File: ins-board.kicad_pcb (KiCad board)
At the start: 4 copper layers, 50 x 23 mm, 93 parts, among them P1 POWER, Q1 FDN306P, Q2 FDC638APZ, U1 24LC128, U10 HMC5883L, U11 H3LIS331DL, U2 STM32F415RGT6, U3 LTC4412, U4 MAX3051, U5 LT1965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

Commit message: signal routing
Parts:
- R15: moved to F.Cu
- moved U4 7.37 mm to (66.9, 45.6)
- moved C11 2.70 mm to (70.2, 47.2), turned to 270 degrees
- moved R15 2.35 mm to (65.8, 47.1), turned to 0 degrees
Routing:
- net /STM32F4_NRST: track 0.00 -> 30.4 mm, vias 0 -> 2
- net /USB_DP: track 0.00 -> 15.8 mm, vias 0 -> 1
- net /V_USB: track 0.00 -> 15.5 mm, vias 0 -> 1
- net /USB_DM: track 0.00 -> 14.8 mm, vias 0 -> 1
- net /STM32F4_TMS: track 0.00 -> 12.9 mm, vias 0 -> 2
- net /Sensors/I2C_SCL: track 0.00 -> 12.7 mm, vias 0 -> 1
- net /Sensors/I2C_SDA: track 0.00 -> 11.4 mm, vias 0 -> 1
- net /UART_CONN3_TX: track 24.7 -> 20.8 mm, vias 1 -> 3
- net /UART_CONN3_RX: track 17.1 -> 19.8 mm, vias 0 -> 1
- net /CAN_CONN1_TX: track 0.00 -> 2.41 mm, vias 0 -> 1
- net /CAN_CONN1_RX: track 0.00 -> 0.99 mm, vias 0 -> 1
- net /Sensors/SPI_MISO: track 13.8 -> 14.7 mm
- net /Sensors/SPI_SCK: track 23.2 -> 22.3 mm
- net /Sensors/SPI_MOSI: track 23.0 -> 22.3 mm

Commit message: signal routing
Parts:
- moved R18 7.76 mm to (56.9, 47.5)
- moved C19 4.23 mm to (68.1, 46.9)
- moved C28 1.04 mm to (53.2, 44.2)
- moved U4 0.36 mm to (66.6, 45.8)
- moved C11 0.11 mm to (70.2, 47.4)
- moved R15 0.07 mm to (65.8, 47.1)
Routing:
- net N-0000059: track 0.00 -> 10.8 mm
- net /CAN_CONN1_RX: track 0.99 -> 10.3 mm
- net N-0000058: track 0.00 -> 9.27 mm
- net /Sensors/I2C_SDA: track 11.4 -> 18.5 mm
- net /CAN_CONN1_TX: track 2.41 -> 7.07 mm
- net N-000006: track 0.00 -> 4.40 mm, vias 0 -> 1
- net /Sensors/I2C_SCL: track 12.7 -> 16.9 mm
- net N-0000085: track 0.00 -> 3.75 mm, vias 0 -> 1
- net N-000003: track 3.16 -> 0.00 mm, vias 1 -> 0
- net /CAN_CONN1_EN: track 0.00 -> 1.93 mm

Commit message: signal routing
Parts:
- moved U4 1.82 mm to (66.0, 44.1)
- moved C19 1.57 mm to (67.5, 45.4)
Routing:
- net N-0000059: track 10.8 -> 0.00 mm
- net /CAN_CONN1_RX: track 10.3 -> 0.00 mm, vias 1 -> 0
- net N-0000058: track 9.27 -> 0.00 mm
- net /CAN_CONN1_TX: track 7.07 -> 0.00 mm, vias 1 -> 0
- net N-000006: track 4.40 -> 0.00 mm, vias 1 -> 0
- net /UART_CONN2_TX: track 20.1 -> 19.4 mm
- net /UART_CONN3_RX: track 19.8 -> 20.4 mm

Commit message: signal routing
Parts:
- R15: moved to B.Cu
- moved C11 3.91 mm to (72.7, 50.4)
- moved R15 0.66 mm to (65.7, 47.8)
- moved U4 0.54 mm to (66.2, 44.5)
- moved C19 0.49 mm to (67.7, 45.9)
- moved C6 0.30 mm to (70.0, 47.2), turned to 0 degrees
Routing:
- net /I2C_CONN1_SDA: track 0.00 -> 39.0 mm, vias 0 -> 2
- net /I2C_CONN1_SCL: track 0.00 -> 36.7 mm, vias 0 -> 2
- net N-0000058: track 0.00 -> 33.6 mm
- net N-0000059: track 0.00 -> 33.4 mm
- net /CAN_CONN1_RX: track 0.00 -> 10.2 mm, vias 0 -> 1
- net /CAN_CONN1_TX: track 0.00 -> 6.61 mm, vias 0 -> 1
- net N-000006: track 0.00 -> 4.15 mm
- net GND: track 40.1 -> 41.6 mm
- net VCC: track 14.6 -> 13.8 mm, vias 4 -> 3
- net /CAN_CONN1_EN: track 1.93 -> 2.69 mm, vias 0 -> 1

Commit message: signal routing
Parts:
- C11: moved to F.Cu
- moved C11 4.58 mm to (69.1, 47.5)
- moved C13 2.40 mm to (43.7, 41.5), turned to 180 degrees
- moved C6 0.57 mm to (70.5, 47.0), turned to 270 degrees
- moved F1 0.48 mm to (49.5, 31.4)
- moved C31 0.37 mm to (49.9, 44.9), turned to 0 degrees
- moved C28 0.28 mm to (53.0, 44.4)
- moved D6 0.16 mm to (47.1, 31.4)
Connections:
- U2 pad 26: /IO_EN -> /Sensors/HMC5883L_DRDY
- U2 pad 28: (no net) -> /IO_EN
- U2 pad 3: /Sensors/HMC5883L_DRDY -> (no net)
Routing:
- net /Sensors/HMC5883L_DRDY: track 0.00 -> 27.4 mm, vias 0 -> 2
- net /Sensors/I2C_SCL: track 16.9 -> 29.6 mm, vias 1 -> 2
- net /Sensors/I2C_SDA: track 18.5 -> 28.0 mm, vias 1 -> 5
- net N-0000077: track 2.43 -> 9.93 mm
- net GND: track 41.6 -> 46.1 mm, vias 7 -> 8
- net N-0000084: track 0.00 -> 2.58 mm, vias 0 -> 1
- net VCC: track 13.8 -> 16.3 mm, vias 3 -> 4
- net /V_USB: track 15.5 -> 17.3 mm, vias 1 -> 2
- net N-000003: track 0.00 -> 1.39 mm
- net N-0000085: track 3.75 -> 2.36 mm
- net /UART_CONN3_RX: track 20.4 -> 19.5 mm
- net /Sensors/MPU6000_FSYNC: track 11.4 -> 10.8 mm
- net /UART_CONN3_TX: track 21.1 -> 21.6 mm

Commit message: signal routing
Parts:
- D1, D3, D4, D5, R1, R7, R8, R9: moved to B.Cu
- moved R14 30.8 mm to (71.7, 32.1)
- moved D1 21.6 mm to (72.9, 32.1), turned to 90 degrees
- moved R1 20.8 mm to (71.4, 32.1), turned to 270 degrees
- moved D4 18.7 mm to (72.0, 40.6), turned to 180 degrees
- moved R11 17.9 mm to (48.2, 39.8), turned to 90 degrees
- moved R10 17.8 mm to (47.5, 37.0), turned to 270 degrees
- moved D3 16.3 mm to (74.0, 35.1), turned to 90 degrees
- moved D5 16.1 mm to (74.2, 37.9), turned to 90 degrees
- moved R8 14.7 mm to (72.0, 39.1)
- moved R9 14.6 mm to (72.1, 37.5)
- moved R7 14.3 mm to (72.1, 36.0)
- moved Q1 12.4 mm to (53.4, 33.0), turned to 90 degrees
- moved D2 12.3 mm to (89.4, 24.3)
- moved R6 12.3 mm to (85.7, 24.4)
- moved C2 0.76 mm to (74.2, 35.1)
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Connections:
- U2 pad 36: /STATUS_LED -> /SD_LED
- U2 pad 43: /SD_LED -> /STATUS_LED
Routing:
- net /SD_LED: track 0.00 -> 12.4 mm, vias 0 -> 1
- net /SD_PWR: track 0.00 -> 11.4 mm, vias 0 -> 1
- net /ERROR_LED: track 0.00 -> 7.91 mm
- net VCC: track 16.3 -> 23.6 mm, vias 4 -> 6
- net GND: track 46.1 -> 51.7 mm, vias 8 -> 12
- net /SDIO_D3: track 8.21 -> 13.7 mm
- net /Sensors/I2C_SCL: track 29.6 -> 32.7 mm, vias 2 -> 3
- net /SDIO_D2: track 7.21 -> 4.32 mm
- net N-000004: track 0.00 -> 1.85 mm
- net N-000001: track 0.00 -> 0.90 mm
- net /UART_CONN4_RX: track 15.6 -> 16.4 mm
- net /UART_CONN4_TX: track 15.1 -> 15.7 mm
- net /Sensors/I2C_SDA: track 28.0 -> 27.8 mm, vias 5 -> 4

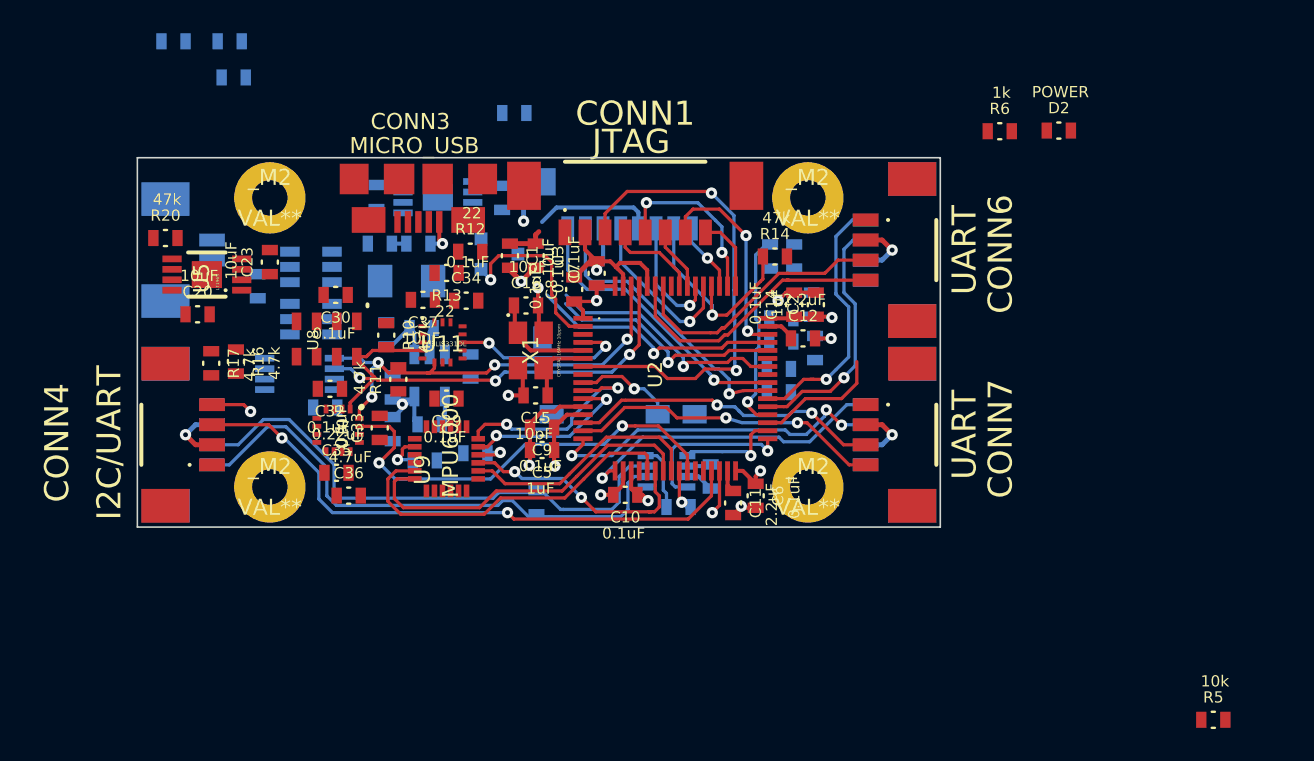
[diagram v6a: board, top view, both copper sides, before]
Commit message: signal routing, all components placed
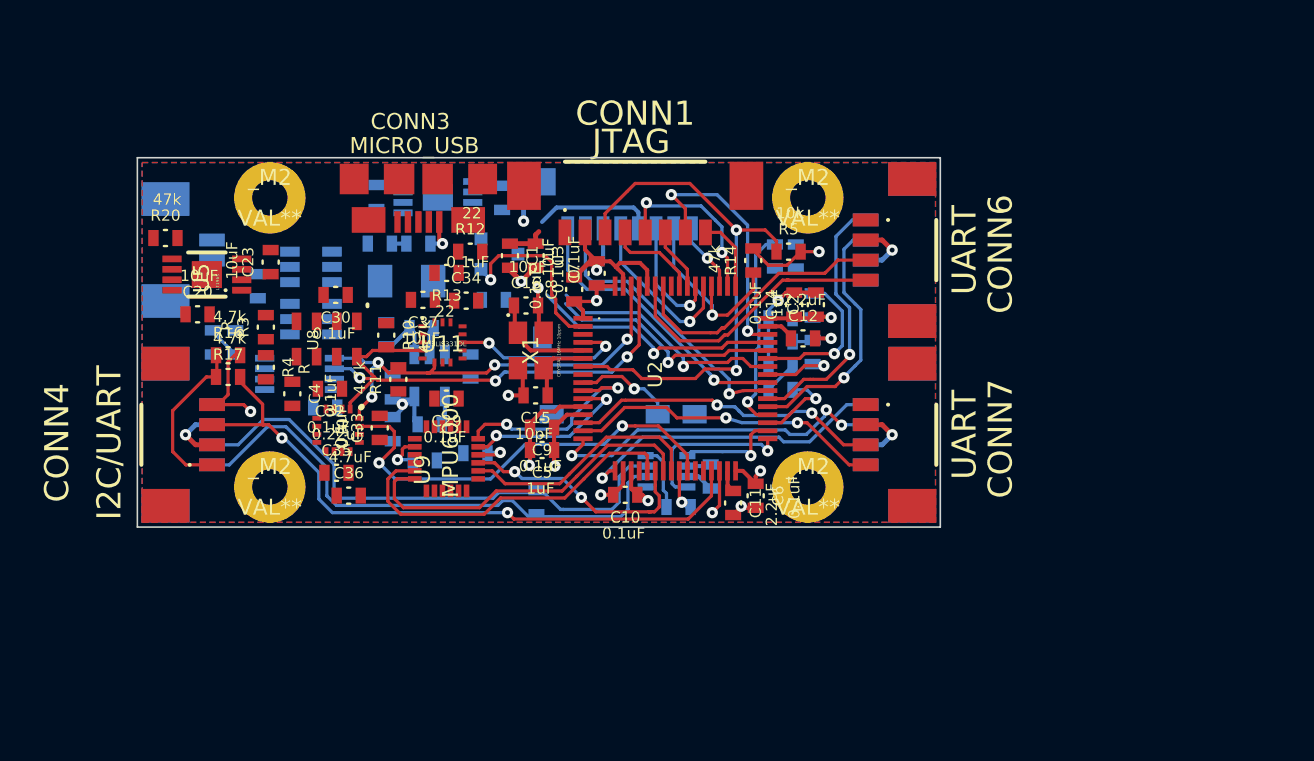
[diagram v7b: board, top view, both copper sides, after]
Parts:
- C4, R3, R4: moved to F.Cu
- D2, R6: moved to B.Cu
- moved D2 54.3 mm to (36.7, 37.5), turned to 270 degrees
- moved R6 49.4 mm to (38.1, 37.5), turned to 270 degrees
- moved R5 39.4 mm to (72.5, 31.9)
- moved R4 20.4 mm to (40.0, 39.0), turned to 270 degrees
- moved C4 20.0 mm to (41.6, 40.7), turned to 270 degrees
- moved R3 18.7 mm to (40.0, 36.5), turned to 90 degrees
- moved R2 11.7 mm to (54.2, 34.9), turned to 180 degrees
- moved R14 1.37 mm to (70.3, 32.4), turned to 90 degrees
- moved R17 1.35 mm to (37.6, 39.6), turned to 0 degrees
- moved R16 0.63 mm to (37.6, 38.3), turned to 0 degrees
- moved R1 0.30 mm to (71.7, 32.1)
- moved D5 0.29 mm to (74.0, 38.1)
- moved R8 0.22 mm to (72.0, 39.0), turned to 180 degrees
- moved D4 0.18 mm to (72.0, 40.5)
- moved D1 0.10 mm to (73.0, 32.1)
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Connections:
- D3 pad 1: N-0000048 -> /ERROR_LED
- D3 pad 2: GND -> N-0000047
- D4 pad 1: N-0000036 -> /STATUS_LED
- D4 pad 2: GND -> N-0000036
- D5 pad 1: N-0000029 -> /HEARTBEAT_LED
- D5 pad 2: GND -> N-0000031
- R7 pad 1: /ERROR_LED -> N-0000047
- R7 pad 2: N-0000048 -> GND
- R8 pad 1: /STATUS_LED -> N-0000036
- R8 pad 2: N-0000036 -> GND
- R9 pad 1: /HEARTBEAT_LED -> N-0000031
- R9 pad 2: N-0000029 -> GND
- U2 pad 35: /ERROR_LED -> /STATUS_LED
- U2 pad 41: (no net) -> /HEARTBEAT_LED
- U2 pad 43: /STATUS_LED -> /ERROR_LED
- U2 pad 57: /HEARTBEAT_LED -> (no net)
- _M2 pad 1: (no net) -> GND (x4)
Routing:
- net /VCC_IO: track 0.00 -> 10.4 mm
- net /STATUS_LED: track 0.00 -> 5.30 mm, vias 0 -> 1
- net VCC: track 23.6 -> 28.5 mm, vias 6 -> 7
- net /HEARTBEAT_LED: track 0.00 -> 4.47 mm, vias 0 -> 1
- net GND: track 51.7 -> 56.0 mm
- net /I2C_CONN1_SDA: track 39.0 -> 43.2 mm
- net /I2C_CONN1_SCL: track 36.7 -> 40.4 mm
- net /STM32F4_NRST: track 30.2 -> 33.8 mm
- net /STM32F4_TMS: track 12.9 -> 16.2 mm
- net N-0000036: track 0.00 -> 2.12 mm
- net N-000009: track 0.00 -> 2.08 mm
- net /ERROR_LED: track 7.91 -> 9.44 mm, vias 0 -> 1
- net N-0000031: track 0.00 -> 1.29 mm
- net N-0000047: track 0.00 -> 1.27 mm
- net /SDIO_D3: track 13.7 -> 12.5 mm
- added copper zone on B.Cu, net GND
- added copper zone on F.Cu, net GND

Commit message: signal routing
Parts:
- R15: moved to F.Cu
- moved R2 3.85 mm to (52.4, 31.4), turned to 270 degrees
- moved R15 0.82 mm to (65.9, 47.0), turned to 180 degrees
- moved Q1 0.49 mm to (53.8, 32.6)
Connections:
- U2 pad 27: /EN_VCC_A -> (no net)
- U2 pad 3: (no net) -> /EN_VCC_A
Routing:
- net /V_BAT_MON_AD: track 0.00 -> 36.6 mm, vias 0 -> 3
- net /EN_VCC_A: track 0.00 -> 13.7 mm, vias 0 -> 1
- net /V_USB: track 17.7 -> 27.3 mm
- net VCC: track 28.5 -> 37.5 mm
- net /USB_DM: track 14.8 -> 19.1 mm
- net /SD_PWR: track 11.4 -> 13.0 mm
- net /Sensors/I2C_SCL: track 32.7 -> 34.3 mm
- net /Sensors/H3LIS331DL_INT1: track 11.1 -> 12.5 mm
- net N-0000077: track 9.93 -> 11.2 mm, vias 0 -> 2
- net N-000003: track 4.15 -> 5.35 mm, vias 0 -> 1
- net /CAN_CONN1_EN: track 2.69 -> 1.70 mm, vias 1 -> 0
- net N-0000061: track 33.6 -> 32.7 mm
- net N-0000062: track 33.4 -> 32.4 mm
- net GND: track 56.0 -> 56.4 mm, vias 12 -> 13
